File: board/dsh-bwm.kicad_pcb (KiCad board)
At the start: 2 copper layers, 136.5 x 78.7 mm, 37 parts, among them IC1 MP4462DN-Z-LF, IC2 MAX485CSA+T, J1 MPM-15-24, J2 Power, J3 Connections, J4 LED, K1 833H-1C-C-24VDC, K2 833H-1C-C-24VDC, K3 833H-1C-C-24VDC, K4 833H-1C-C-24VDC, Q1 IRLB8721PBF, U1 Pico

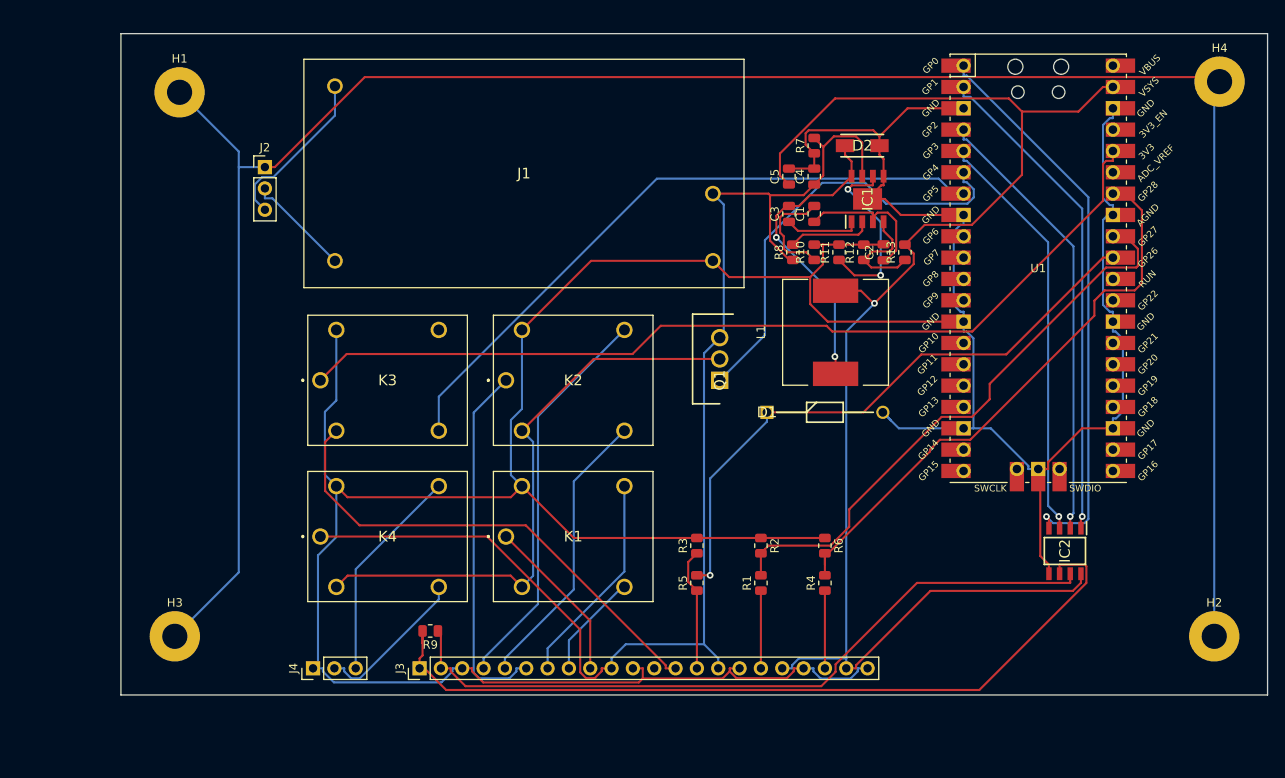
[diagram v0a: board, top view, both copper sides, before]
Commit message: Redo traces - MPS fixes
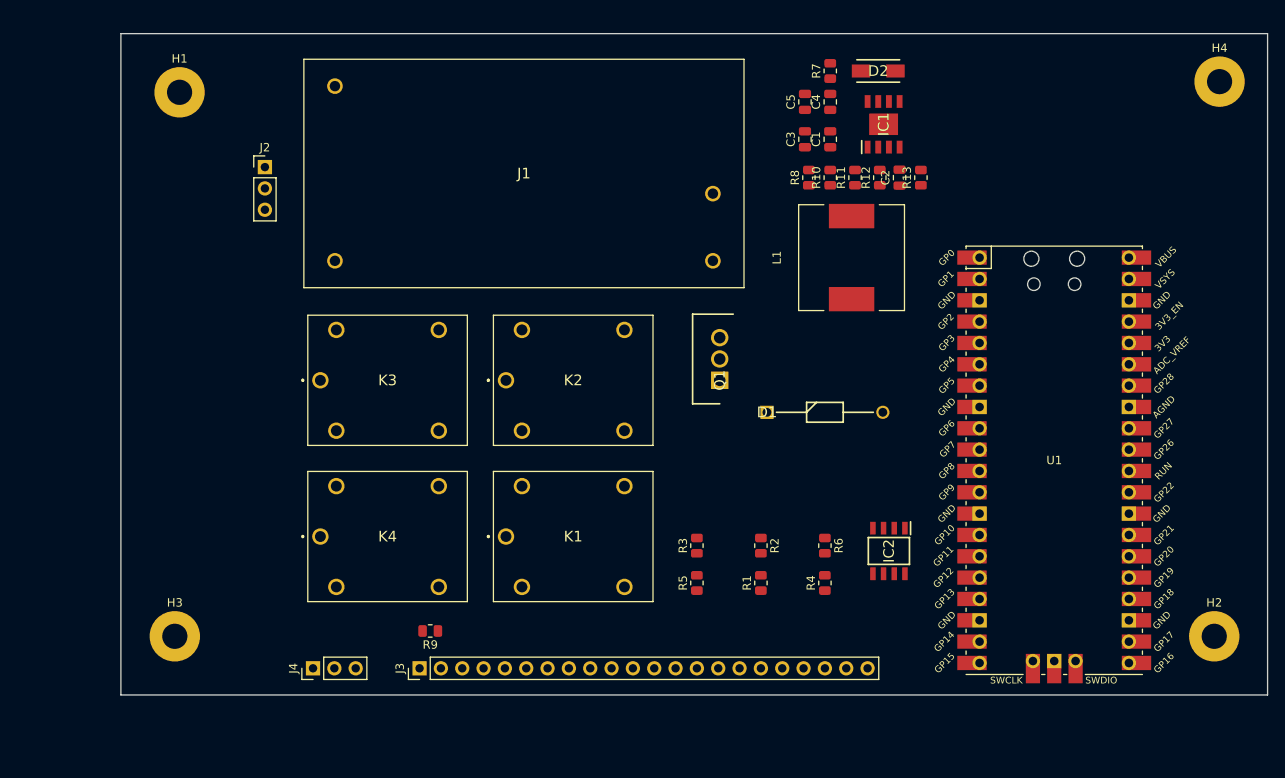
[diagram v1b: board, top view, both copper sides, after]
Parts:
- moved U1 22.9 mm to (200.7, 106.0)
- moved IC2 21.0 mm to (181.0, 116.8)
- moved C4 9.09 mm to (174.0, 63.4)
- moved C5 9.09 mm to (171.0, 63.4)
- moved C1 9.09 mm to (174.0, 67.8)
- moved C2 9.09 mm to (182.2, 72.4)
- moved C3 9.09 mm to (171.0, 67.8)
- moved D2 9.09 mm to (179.7, 59.7)
- moved IC1 9.09 mm to (180.3, 66.0)
- moved L1 9.09 mm to (176.5, 81.9)
- moved R10 9.09 mm to (174.0, 72.4)
- moved R11 9.09 mm to (176.9, 72.4)
- moved R13 9.09 mm to (184.8, 72.4)
- moved R7 9.09 mm to (174.0, 59.7)
- moved R8 9.09 mm to (171.4, 72.4)
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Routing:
- net GND: track 439.6 -> 0.00 mm
- net Net-(H1-Pad1): track 258.6 -> 0.00 mm
- net 5V: track 174.5 -> 0.00 mm, vias 1 -> 0
- net 24V: track 154.6 -> 0.00 mm
- net 3v3: track 109.5 -> 0.00 mm
- net A: track 98.4 -> 0.00 mm
- net B: track 87.6 -> 0.00 mm
- net ZD: track 78.0 -> 0.00 mm
- net COND: track 72.6 -> 0.00 mm, vias 1 -> 0
- net PSin: track 70.3 -> 0.00 mm
- net Net-(K1-Pad2): track 70.0 -> 0.00 mm
- net PSout: track 69.1 -> 0.00 mm
- net DI: track 67.4 -> 0.00 mm, vias 1 -> 0
- net RO: track 58.9 -> 0.00 mm, vias 1 -> 0
- net ZDSENSE: track 58.4 -> 0.00 mm
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
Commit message: Traces, traces everywhere
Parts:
- moved R9 61.1 mm to (187.3, 121.4)
- moved C4 22.4 mm to (186.2, 82.2), turned to -90 degrees
- moved R7 22.0 mm to (174.4, 81.7), turned to 0 degrees
- moved R12 19.3 mm to (174.2, 90.8), turned to 180 degrees
- moved R13 18.8 mm to (174.2, 88.0), turned to 180 degrees
- moved D2 18.7 mm to (185.4, 77.5), turned to 180 degrees
- moved R10 17.9 mm to (178.3, 89.8), turned to 180 degrees
- moved C5 17.2 mm to (185.2, 73.2), turned to 180 degrees
- moved IC1 16.5 mm to (180.1, 82.5), turned to 0 degrees
- moved R11 16.1 mm to (185.2, 86.2), turned to -90 degrees
- moved C1 15.9 mm to (174.5, 83.7), turned to 180 degrees
- moved J4 14.2 mm to (126.3, 127.8)
- moved J3 14.2 mm to (138.9, 127.8)
- moved L1 13.4 mm to (173.7, 68.8)
- moved C3 12.5 mm to (178.6, 77.7), turned to 0 degrees
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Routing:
- net GND: track 0.00 -> 409.3 mm
- net Net-(H1-Pad1): track 0.00 -> 263.4 mm
- net 24V: track 0.00 -> 160.3 mm
- net 5V: track 0.00 -> 117.4 mm, vias 0 -> 2
- net 3v3: track 0.00 -> 87.4 mm
- net ZD: track 0.00 -> 86.5 mm
- net A: track 0.00 -> 77.4 mm
- net B: track 0.00 -> 71.0 mm
- net Net-(K1-Pad2): track 0.00 -> 70.0 mm
- net ZDSENSE: track 0.00 -> 64.9 mm
- net ALARM: track 0.00 -> 63.8 mm
- net COND: track 0.00 -> 57.0 mm, vias 0 -> 1
- net Net-(C1-Pad1): track 0.00 -> 43.3 mm
- net AlarmC2: track 0.00 -> 43.2 mm
- net PSin: track 0.00 -> 38.6 mm, vias 0 -> 1
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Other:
- board size 136.5 x 78.7 mm -> 133.5 x 78.7 mm

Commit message: Bigger is better?
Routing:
- net GND: track 409.3 -> 462.7 mm
- net 5V: track 117.4 -> 162.0 mm, vias 2 -> 1
- net L1: track 22.6 -> 38.6 mm
- net 24V: track 160.3 -> 171.3 mm, vias 0 -> 1
- net ZD: track 86.5 -> 96.9 mm
- net Net-(C1-Pad1): track 43.3 -> 36.1 mm, vias 0 -> 2
- net ALARM: track 63.8 -> 56.6 mm
- net AlarmC2: track 43.2 -> 50.1 mm
- net RE: track 32.3 -> 38.9 mm, vias 0 -> 1
- net B: track 71.0 -> 74.9 mm
- net Net-(IC1-Pad2): track 3.79 -> 0.00 mm
- net Net-(H1-Pad1): track 263.4 -> 267.2 mm
- net A: track 77.4 -> 81.1 mm
- net Net-(C1-Pad2): track 16.8 -> 13.2 mm, vias 0 -> 2
- net ZDSENSE: track 64.9 -> 68.5 mm, vias 0 -> 2
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
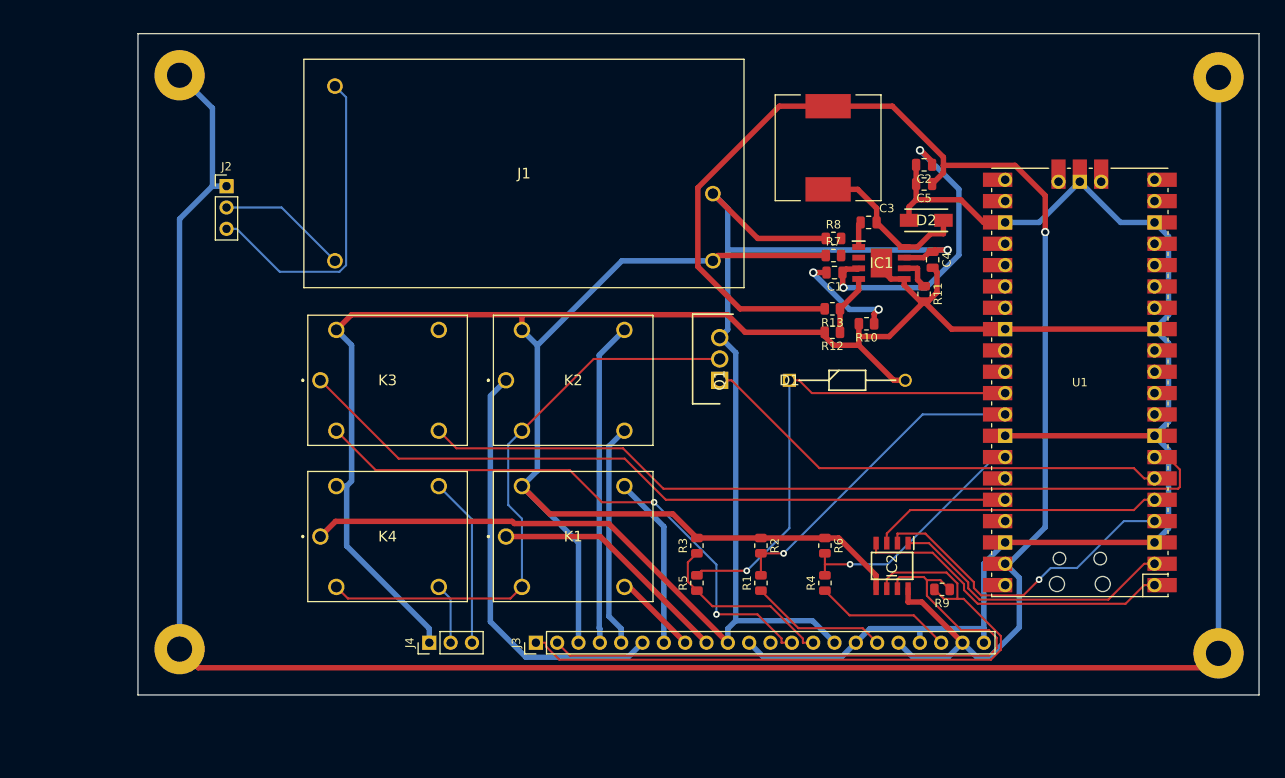
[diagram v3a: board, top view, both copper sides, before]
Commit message: Fix unrouted, thanks Emiel
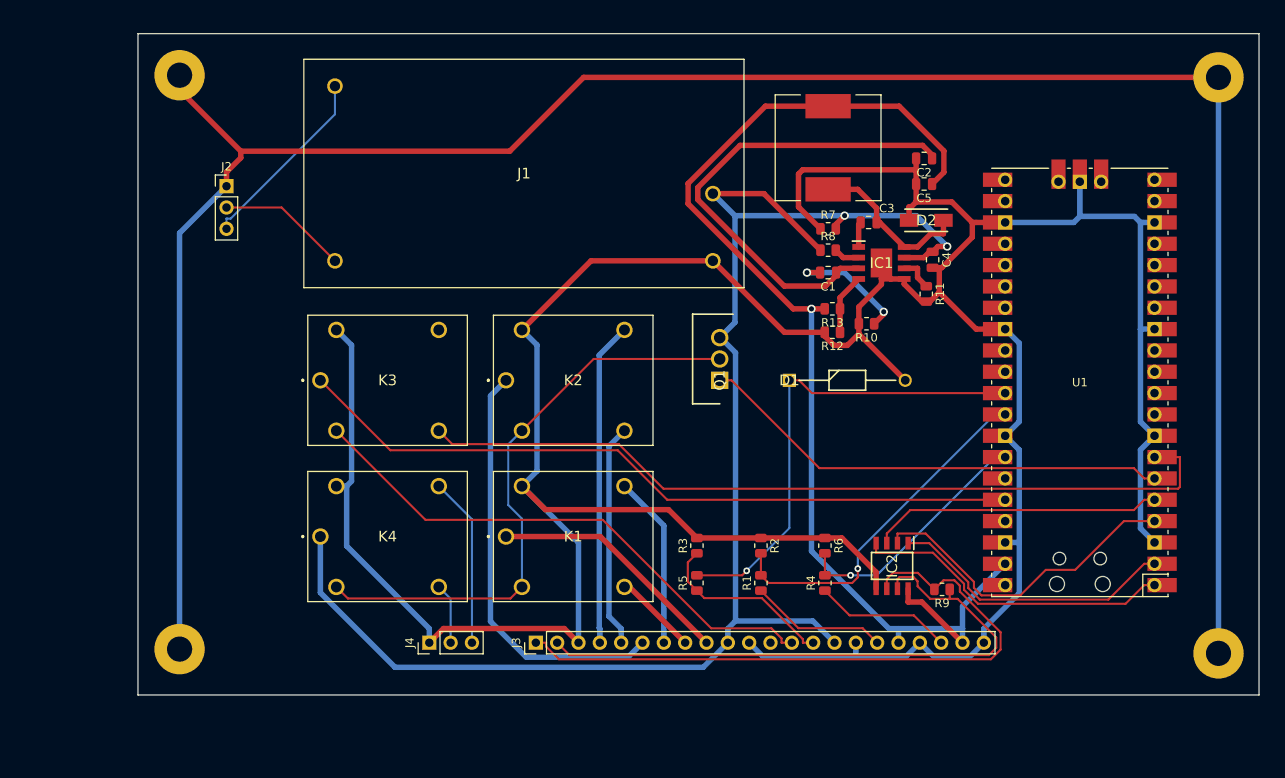
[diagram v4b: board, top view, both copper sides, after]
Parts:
- moved R7 3.24 mm to (173.7, 78.5)
- moved R8 1.53 mm to (173.7, 81.0)
- moved C1 0.76 mm to (173.7, 83.7)
- moved C2 0.76 mm to (185.2, 70.1)
- moved R11 0.25 mm to (185.4, 86.2)
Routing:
- net GND: track 462.7 -> 428.8 mm
- net 5V: track 162.0 -> 138.8 mm
- net Net-(C1-Pad1): track 36.1 -> 56.8 mm, vias 2 -> 0
- net L1: track 38.6 -> 22.6 mm
- net 24V: track 171.3 -> 179.5 mm, vias 1 -> 2
- net Net-(H1-Pad1): track 267.2 -> 263.0 mm
- net PSin: track 38.6 -> 42.2 mm
- net ZDSENSE: track 68.5 -> 65.0 mm, vias 2 -> 0
- net Net-(IC1-Pad2): track 0.00 -> 3.09 mm
- net B: track 74.9 -> 71.9 mm
- net A: track 81.1 -> 78.2 mm
- net Net-(C1-Pad2): track 13.2 -> 14.5 mm
- net ZD: track 96.9 -> 97.8 mm
- net PSout: track 29.4 -> 29.9 mm
- net RE: vias 1 -> 0

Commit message: RP2040 Stamp
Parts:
- removed R10: 100K, Resistor_SMD:R_0805_2012Metric
- removed R11: 200k, Resistor_SMD:R_0805_2012Metric
- removed R12: 40.2k, Resistor_SMD:R_0805_2012Metric
- removed R13: 210k, Resistor_SMD:R_0805_2012Metric
- added C6: 0.01uF, Capacitor_SMD:C_0805_2012Metric, F.Cu at (173.6, 73.8)
- added J5: SWD6p, Connector_PinHeader_2.54mm:PinHeader_2x03_P2.54mm_Vertical, F.Cu at (158.5, 103.6)
- added SW1: BOOTSEL, Button_Switch_SMD:SW_SPST_B3U-1000P, F.Cu at (189.7, 82.3)
- C1: value 150pF -> 4.7uF
- C2: value NS -> 4.7uF
- C3: value 100nF -> 0.01uF
- C4: value 10uF -> 0.01uF
- C5: value 22uF -> 330uF; footprint Capacitor_SMD:C_0805_2012Metric -> SamacSys_Parts:POSCAP_D12_D15_D15E_D2E_D2_D3L_D4
- D2: value lowfd -> B540C; footprint SamacSys_Parts:DIONM5127X229N -> SamacSys_Parts:DIOM7959X250N
- IC1: value MP4462DN-Z-LF -> TPS5450DDA
- L1: value 22uH -> 15uH; footprint Inductor_SMD:L_12x12mm_H4.5mm -> SamacSys_Parts:INDPM120120X800N
- R7: value 17.4k -> 10k
- R8: value 100K -> 3.16k
- U1: value Pico -> RP2040_Stamp; footprint MCU_RaspberryPi_and_Boards:RPi_Pico_SMD_TH -> SamacSys_Parts:RP2040_Stamp_SMD
- moved IC1 28.4 mm to (197.9, 60.5)
- moved U1 23.3 mm to (180.6, 99.3), turned to 0 degrees
- moved C3 19.9 mm to (194.7, 66.0)
- moved C2 16.3 mm to (169.2, 72.9), turned to 0 degrees
- moved D1 13.5 mm to (168.4, 83.1)
- moved H2 12.7 mm to (207.5, 129.0)
- moved H4 12.7 mm to (207.5, 60.5)
- moved C5 12.6 mm to (188.0, 60.9), turned to 0 degrees
- moved C4 12.3 mm to (178.1, 72.9), turned to 0 degrees
- moved R8 10.1 mm to (182.5, 75.9)
- moved D2 9.21 mm to (187.1, 68.4), turned to 0 degrees
- moved C1 9.00 mm to (169.2, 75.9), turned to 0 degrees
- moved R7 5.02 mm to (178.0, 75.9)
- moved L1 4.57 mm to (174.3, 64.3), turned to 0 degrees
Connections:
- C1 pad 1: Net-(C1-Pad1) -> 24V
- C1 pad 2: Net-(C1-Pad2) -> GND
- C2 pad 1: Net-(C1-Pad1) -> 24V
- C3 pad 1: Net-(C3-Pad1) -> 24V
- C3 pad 2: Net-(C3-Pad2) -> GND
- C4 pad 1: 24V -> Net-(C4-Pad1)
- C4 pad 2: GND -> Net-(C4-Pad2)
- D2 pad 1: Net-(C3-Pad2) -> 5V
- IC1 pad 1: Net-(C3-Pad1) -> Net-(C4-Pad1)
- IC1 pad 2: Net-(IC1-Pad2) -> unconnected-(IC1-Pad2)
- IC1 pad 3: Net-(C1-Pad1) -> unconnected-(IC1-Pad3)
- IC1 pad 5: GND -> unconnected-(IC1-Pad5)
- IC1 pad 6: Net-(IC1-Pad6) -> GND
- IC1 pad 8: Net-(C3-Pad2) -> Net-(C4-Pad2)
- L1 pad 1: Net-(C3-Pad2) -> Net-(C4-Pad2)
- R7 pad 1: GND -> Net-(IC1-Pad4)
- R7 pad 2: 24V -> 5V
- R8 pad 1: 24V -> GND
- R8 pad 2: Net-(IC1-Pad2) -> Net-(IC1-Pad4)
- U1 pad 1: DI -> unconnected-(U1-Pad1)
- U1 pad 13: GND -> unconnected-(U1-Pad13)
- U1 pad 18: GND -> unconnected-(U1-Pad18)
- U1 pad 2: RO -> unconnected-(U1-Pad2)
- U1 pad 23: GND -> unconnected-(U1-Pad23)
- U1 pad 27: unconnected-(U1-Pad27) -> COND
- U1 pad 28: GND -> PSin
- U1 pad 29: unconnected-(U1-Pad29) -> PSout
- U1 pad 3: GND -> RE
- U1 pad 31: COND -> GND
- U1 pad 32: PSin -> unconnected-(U1-Pad32)
- U1 pad 33: GND -> 5V
- U1 pad 34: PSout -> 3v3
- U1 pad 36: 3v3 -> unconnected-(U1-Pad36)
- U1 pad 37: unconnected-(U1-Pad37) -> SWDIO
- U1 pad 38: GND -> SWCLK
- U1 pad 39: 5V -> RESET
- U1 pad 4: RE -> DE
- U1 pad 40: unconnected-(U1-Pad40) -> Net-(SW1-Pad2)
- U1 pad 5: DE -> DI
- U1 pad 6: ALARM -> RO
- U1 pad 8: GND -> ALARM
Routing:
- net GND: track 428.8 -> 0.00 mm
- net Net-(H1-Pad1): track 263.0 -> 0.00 mm
- net 24V: track 179.5 -> 0.00 mm, vias 2 -> 0
- net 5V: track 138.8 -> 0.00 mm, vias 1 -> 0
- net ZD: track 97.8 -> 0.00 mm
- net 3v3: track 87.4 -> 0.00 mm
- net A: track 78.2 -> 0.00 mm
- net B: track 71.9 -> 0.00 mm
- net Net-(K1-Pad2): track 70.3 -> 0.00 mm
- net ZDSENSE: track 65.0 -> 0.00 mm
- net COND: track 57.3 -> 0.00 mm, vias 1 -> 0
- net Net-(C1-Pad1): track 56.8 -> 0.00 mm
- net ALARM: track 56.6 -> 0.00 mm
- net AlarmC2: track 50.1 -> 0.00 mm
- net PSin: track 42.2 -> 0.00 mm, vias 1 -> 0
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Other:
- board size 133.5 x 78.7 mm -> 121.3 x 78.7 mm

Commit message: Power shit and copper fillz boi
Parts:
- J3: footprint Connector_PinHeader_2.54mm:PinHeader_1x22_P2.54mm_Vertical -> Connector_PinHeader_2.54mm:PinHeader_1x27_P2.54mm_Vertical
- moved R7 27.3 mm to (204.5, 69.2), turned to -90 degrees
- moved R8 22.1 mm to (204.5, 73.7), turned to 90 degrees
- moved C4 22.0 mm to (199.9, 75.4), turned to 180 degrees
- moved L1 20.5 mm to (184.4, 82.2), turned to 180 degrees
- moved IC2 19.7 mm to (200.3, 113.0)
- moved J3 15.5 mm to (123.4, 128.0)
- moved R9 12.6 mm to (199.8, 119.9)
- moved C5 12.5 mm to (179.8, 70.2), turned to 90 degrees
- moved J4 12.2 mm to (114.1, 128.0)
- moved IC1 9.66 mm to (198.4, 70.1), turned to 180 degrees
- moved D1 9.66 mm to (168.7, 92.7)
- moved SW1 9.66 mm to (190.1, 91.9)
- moved R4 9.14 mm to (164.2, 120.7)
- moved R6 9.14 mm to (164.2, 116.2)
- moved U1 9.03 mm to (181.0, 108.3)
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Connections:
- C4 pad 2: Net-(C4-Pad2) -> /Power/5Vunf
- D2 pad 1: 5V -> /Power/5Vunf
- IC1 pad 8: Net-(C4-Pad2) -> /Power/5Vunf
- J5 pad 1: 5V -> UART RX
- J5 pad 3: RESET -> UART TX
- J5 pad 6: unconnected-(J5-Pad6) -> 5V
- L1 pad 1: Net-(C4-Pad2) -> /Power/5Vunf
- R7 pad 2: 5V -> /Power/5Vunf
- U1 pad 1: unconnected-(U1-Pad1) -> UART TX
- U1 pad 10: unconnected-(U1-Pad10) -> LDNC
- U1 pad 2: unconnected-(U1-Pad2) -> UART RX
- U1 pad 9: unconnected-(U1-Pad9) -> LDNO
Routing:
- net GND: track 0.00 -> 307.5 mm, vias 0 -> 13
- net Net-(H1-Pad1): track 0.00 -> 254.6 mm
- net 24V: track 0.00 -> 186.0 mm, vias 0 -> 8
- net 5V: track 0.00 -> 113.6 mm, vias 0 -> 5
- net 3v3: track 0.00 -> 109.9 mm, vias 0 -> 1
- net B: track 0.00 -> 97.3 mm
- net A: track 0.00 -> 88.1 mm
- net Net-(K1-Pad2): track 0.00 -> 70.7 mm, vias 0 -> 1
- net COND: track 0.00 -> 67.5 mm, vias 0 -> 4
- net AlarmC2: track 0.00 -> 54.2 mm
- net ZDSENSE: track 0.00 -> 49.6 mm
- net ZD: track 0.00 -> 45.6 mm
- net AlarmNC2: track 0.00 -> 45.1 mm
- net PSin: track 0.00 -> 44.1 mm, vias 0 -> 2
- net PSout: track 0.00 -> 40.6 mm, vias 0 -> 2
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- added copper zone on F.Cu, net /Power/5Vunf
- added copper zone on F.Cu, net 24V
- added copper zone on F.Cu, net 5V
- added copper zone on F.Cu, net GND
